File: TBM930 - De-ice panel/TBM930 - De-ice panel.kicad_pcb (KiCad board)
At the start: 2 copper layers, 190.5 x 101.6 mm, 81 parts, among them J1 SW_AIRFRAME_DE_ICE, J10 AVR-ISP-6, J2 SW_ICE_LIGHT, J3 SW_PROP_DE_ICE, J4 SW_WIND_SHIELD, J5 SW_PITOT_L_HTR, J6 SW_PITOT_R_HTR, J7 SW_INERT_SEP, J8 Barrel_Jack, J9 USB_B_Micro, SW1 SW_Push, SW2 SW_Push, U1 TLC5917IN, U2 TLC5917IN, U3 ATmega32U4-MU, Y1 16MHz

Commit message: Everything is routed!
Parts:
- removed the C1 at (214.0, 125.1)
- removed the C1 at (160.8, 130.6)
- removed C11, C14: 1uF, Capacitor_SMD:C_0603_1608Metric
- removed C12, C15: 0.1uF, Capacitor_SMD:C_0603_1608Metric
- removed C13: 10uF, Capacitor_SMD:C_0603_1608Metric
- removed D17: LED, LED_SMD:LED_1206_3216Metric_Pad1.42x1.75mm_HandSolder
- added C1: 10uF, Capacitor_SMD:C_0603_1608Metric, B.Cu at (214.0, 125.1)
- added R9: 330, Resistor_SMD:R_0603_1608Metric, B.Cu at (175.1, 131.6)
- FB1: value Ferrite_Bead -> Ferrite_Bead_Small; footprint Resistor_SMD:R_0805_2012Metric -> Capacitor_SMD:C_0805_2012Metric; moved to B.Cu
- R2, R5: footprint Resistor_SMD:R_0201_0603Metric -> Resistor_SMD:R_0603_1608Metric
- Y1: value 16MHz -> Crystal_GND24
- moved D18 95.2 mm to (182.2, 46.4)
- moved D20 95.2 mm to (87.0, 46.4)
- moved D21 95.2 mm to (182.2, 140.3)
- moved D23 95.2 mm to (87.0, 140.3)
- moved D12 63.9 mm to (160.0, 78.1)
- moved FB1 61.2 mm to (223.5, 125.3)
- moved C6 52.7 mm to (209.9, 119.8)
- moved D24 50.8 mm to (43.2, 67.9)
- moved D25 50.8 mm to (43.2, 118.7)
- moved D15 50.8 mm to (210.8, 78.1)
- moved D13 25.4 mm to (134.6, 78.1)
- moved D14 25.4 mm to (109.2, 78.1)
- moved J10 25.2 mm to (180.9, 132.0)
- moved C10 24.7 mm to (221.6, 125.3), turned to 270 degrees
- moved D2 22.2 mm to (197.9, 134.6)
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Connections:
- D16 pad 1: Net-(D16-Pad1) -> BACKLIGHT3
- FB1 pad 1: +12V_LED -> +5V
- FB1 pad 2: /+12V -> Net-(FB1-Pad2)
- J8 pad 1: /+12V -> +12V_LED
- J9 pad 1: +5V -> Net-(FB1-Pad2)
- SW2 pad 1: /~RESET -> Net-(R9-Pad1)
- U1 pad 10: Net-(U1-Pad10) -> PROP
- U1 pad 11: Net-(U1-Pad11) -> WINDSHIELD_1
- U1 pad 12: Net-(U1-Pad12) -> WINDSHIELD_2
- U1 pad 5: WINDSHIELD_2 -> Net-(U1-Pad5)
- U1 pad 6: WINDSHIELD_1 -> Net-(U1-Pad6)
- U1 pad 7: PROP -> Net-(U1-Pad7)
- U1 pad 8: AIRFRAME_2 -> AIRFRAME_1
- U1 pad 9: AIRFRAME_1 -> AIRFRAME_2
- U2 pad 10: BACKLIGHT6 -> BACKLIGHT2
- U2 pad 11: BACKLIGHT7 -> BACKLIGHT3
- U2 pad 5: BACKLIGHT1 -> BACKLIGHT5
- U2 pad 6: BACKLIGHT2 -> BACKLIGHT6
- U2 pad 7: BACKLIGHT3 -> BACKLIGHT4
- U2 pad 8: BACKLIGHT4 -> BACKLIGHT7
- U2 pad 9: BACKLIGHT5 -> BACKLIGHT1
- U3 pad 12: SW_LTS_TEST -> Net-(U3-Pad12)
- U3 pad 18: SW_PITOT_R -> /D3
- U3 pad 25: LED_CLOCK -> LED_LATCH
- U3 pad 26: LED_LATCH -> LED_CLOCK
- U3 pad 36: /A0 -> SW_LTS_TEST
- U3 pad 37: /A1 -> SW_PROP
- U3 pad 38: SW_PROP -> SW_WINDSHIELD
- U3 pad 39: SW_INERT_SEP -> SW_PITOT_L
- U3 pad 40: SW_PITOT_L -> SW_PITOT_R
- U3 pad 41: SW_WINDSHIELD -> SW_INERT_SEP
- Y1 pad 2: /XTAL2 -> GND
- Y1 pad 3: (no net) -> /XTAL2
- Y1 pad 4: (no net) -> GND
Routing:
- net +12V_LED: track 0.00 -> 545.9 mm, vias 0 -> 2
- net BACKLIGHT7: track 0.00 -> 315.9 mm, vias 0 -> 1
- net +5V: track 73.3 -> 377.1 mm, vias 6 -> 8
- net BACKLIGHT4: track 0.00 -> 174.0 mm, vias 0 -> 1
- net SW_AIRFRAME: track 0.00 -> 153.3 mm
- net AIRFRAME_1: track 0.00 -> 127.8 mm, vias 0 -> 4
- net SW_ICE_LIGHT: track 0.00 -> 127.7 mm
- net SW_LTS_TEST: track 2.97 -> 124.1 mm
- net SW_PROP: track 0.00 -> 108.3 mm
- net AIRFRAME_2: track 0.00 -> 107.7 mm, vias 0 -> 2
- net BACKLIGHT3: track 0.00 -> 105.5 mm, vias 0 -> 7
- net LED_LATCH: track 0.00 -> 99.3 mm
- net BACKLIGHT_BRIGHT: track 0.00 -> 96.6 mm, vias 0 -> 2
- net LED_CLOCK: track 0.00 -> 94.9 mm, vias 0 -> 2
- net SW_WINDSHIELD: track 0.00 -> 83.4 mm
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
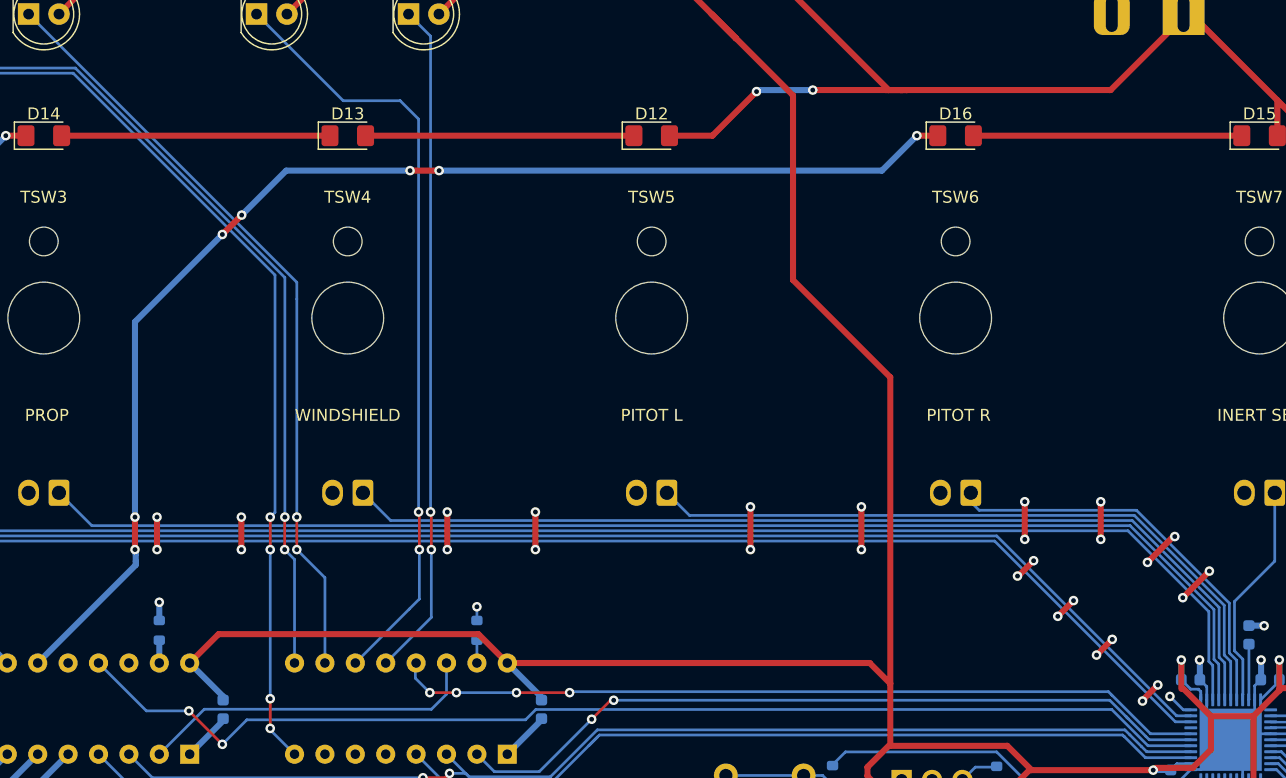
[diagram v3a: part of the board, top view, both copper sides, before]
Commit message: Schematic submitted to microtype
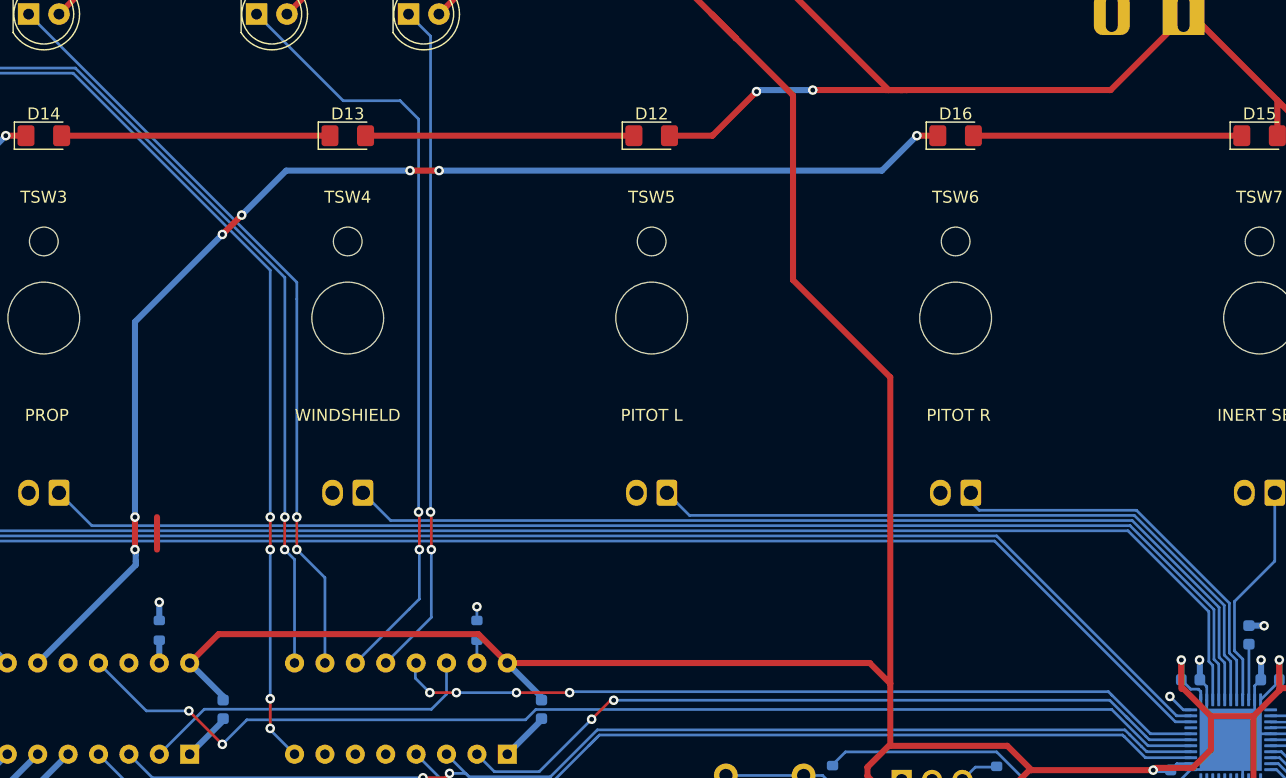
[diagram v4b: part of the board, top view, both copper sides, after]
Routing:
- net GND: track 120.0 -> 82.8 mm, vias 47 -> 19

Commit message: Schematic updates based on MT engineering discord feedback
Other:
- board text added: "JLCJLCJLCJLC"

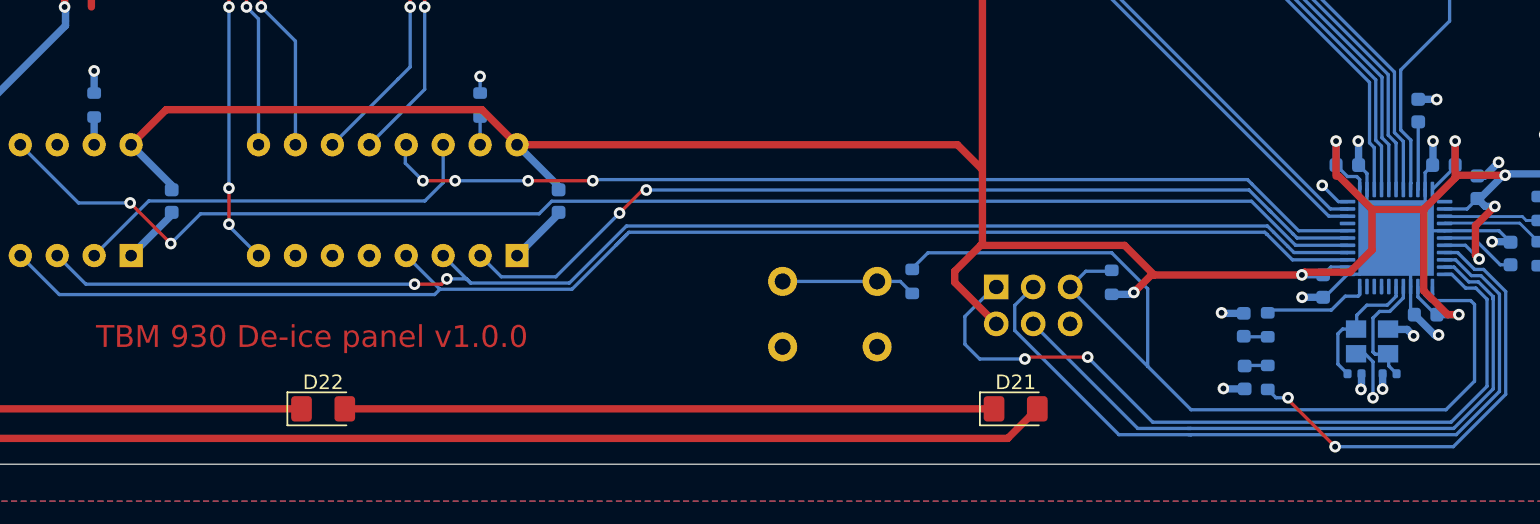
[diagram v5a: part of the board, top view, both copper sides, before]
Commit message: Additional reset components
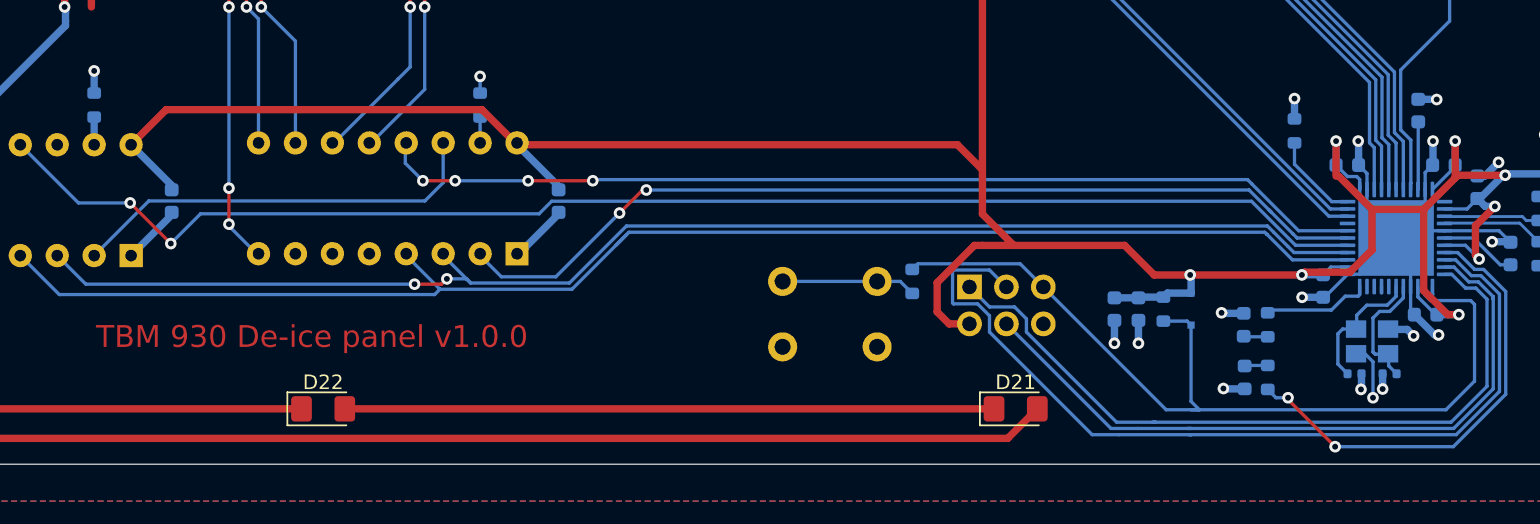
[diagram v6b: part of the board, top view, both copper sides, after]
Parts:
- removed R1: 10K, Resistor_SMD:R_0603_1608Metric
- added C11: 0.1uf, Capacitor_SMD:C_0603_1608Metric, B.Cu at (190.7, 133.5)
- added C12: 0.1uF, Capacitor_SMD:C_0603_1608Metric, B.Cu at (189.0, 133.5)
- added D17: D, Diode_SMD:D_SOD-323F, B.Cu at (194.3, 133.5)
- added R10: 10K, Resistor_SMD:R_0603_1608Metric, B.Cu at (192.4, 133.5)
- added R11: 10K, Resistor_SMD:R_0603_1608Metric, B.Cu at (201.4, 121.2)
- moved J10 1.84 mm to (179.1, 132.0)
- moved U1 0.13 mm to (148.0, 129.7)
- turned R3 to 270 degrees
- turned R4 to 270 degrees
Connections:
- net /~RESET renamed RESET
- R3 pad 1: Net-(R3-Pad1) -> GND
- R3 pad 2: GND -> Net-(R3-Pad2)
- R4 pad 1: Net-(R4-Pad1) -> GND
- R4 pad 2: GND -> Net-(R4-Pad2)
- U1 pad 15: Net-(R3-Pad1) -> Net-(R3-Pad2)
- U2 pad 15: Net-(R4-Pad1) -> Net-(R4-Pad2)
- U3 pad 33: GND -> Net-(R11-Pad1)
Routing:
- net /SCK: track 52.7 -> 61.3 mm
- net Net-(R11-Pad1): track 0.00 -> 6.18 mm
- net RESET: track 68.1 -> 62.0 mm
- net +5V: track 377.1 -> 382.5 mm
- net /MISO: track 53.8 -> 50.8 mm, vias 2 -> 0
- net GND: track 82.8 -> 85.1 mm, vias 19 -> 21
- net Net-(R4-Pad2): track 0.00 -> 1.91 mm
- net Net-(R4-Pad1): track 1.91 -> 0.00 mm
- net Net-(R3-Pad1): track 1.91 -> 0.00 mm
- net /MOSI: track 46.7 -> 48.5 mm
- net Net-(R3-Pad2): track 0.00 -> 1.78 mm

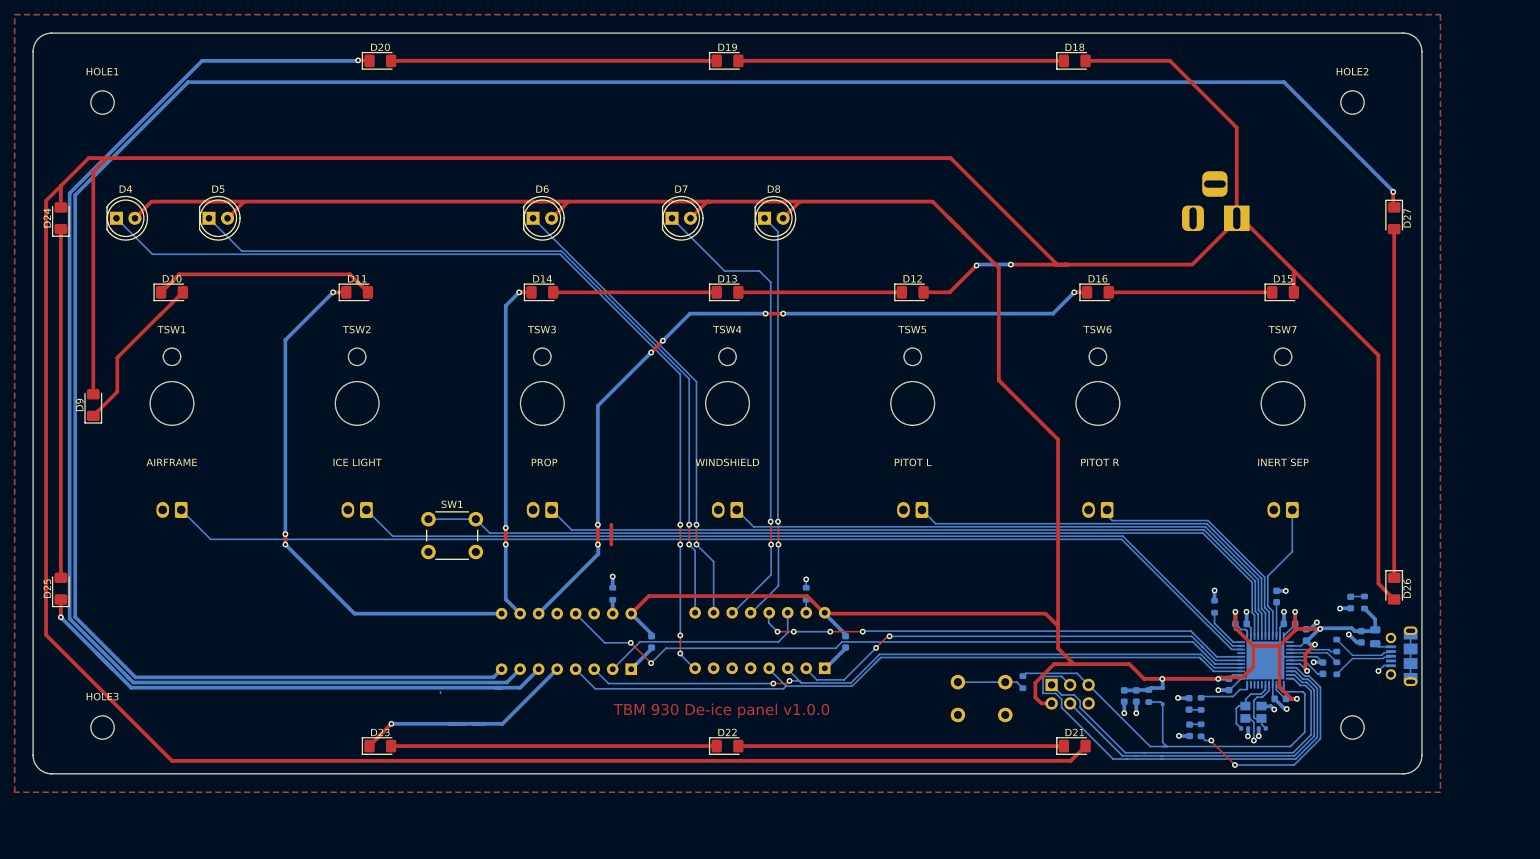
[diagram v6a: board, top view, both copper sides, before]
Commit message: Fix 12V routing
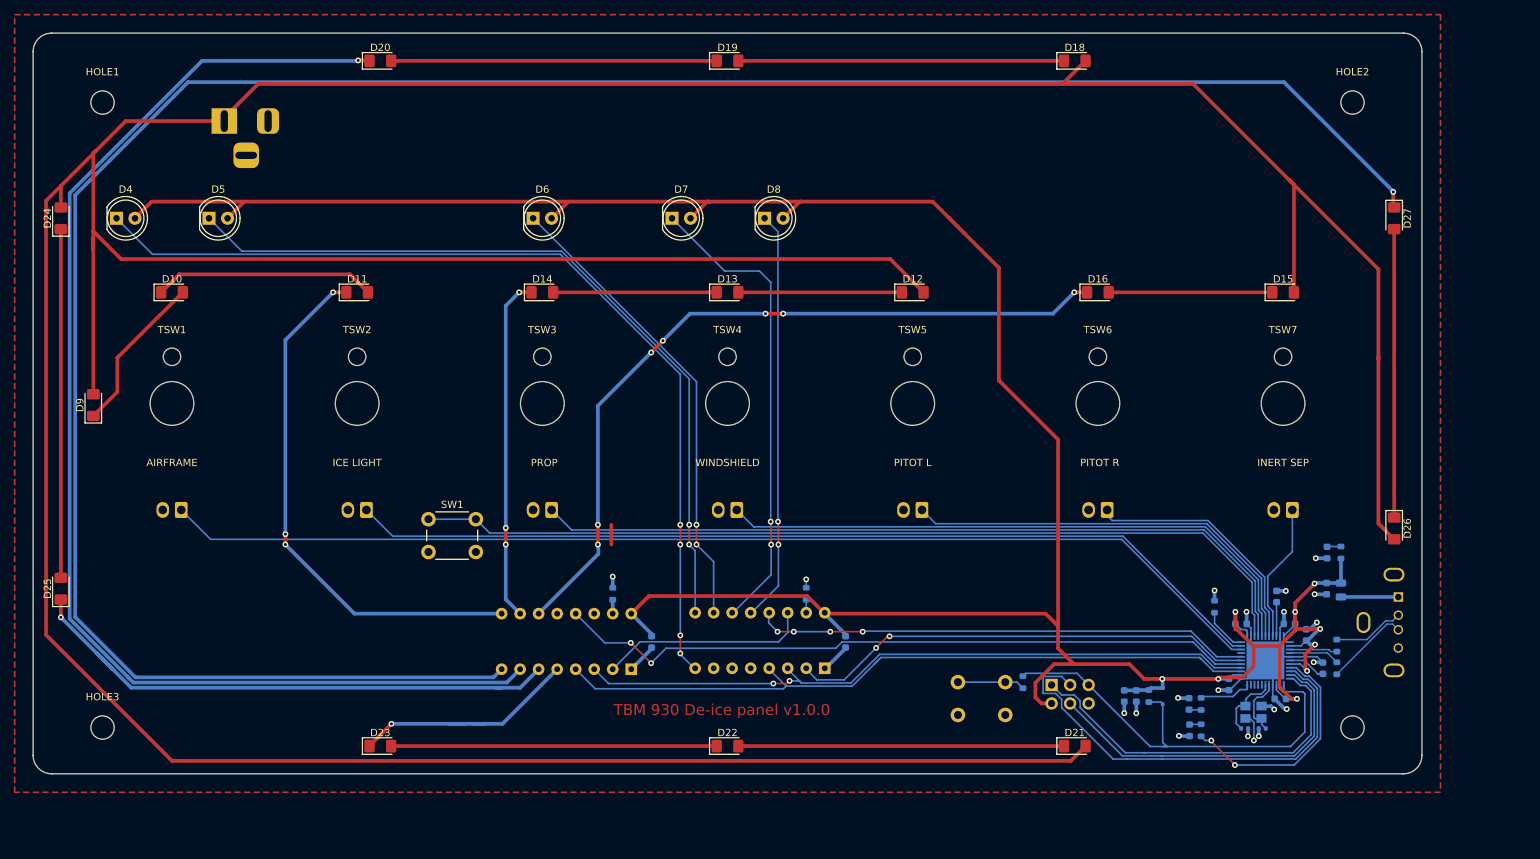
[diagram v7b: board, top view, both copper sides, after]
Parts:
- J9: footprint Connector_USB:USB_Micro-B_Molex-105017-0001 -> Global MobiFlight panel parts:USB_A_Molex_105057_Vertical
- moved J8 139.5 mm to (65.6, 54.6), turned to 180 degrees
- moved D26 8.26 mm to (226.1, 110.5)
- moved C10 8.14 mm to (216.8, 118.7)
- moved J9 8.14 mm to (226.6, 119.9)
- moved FB1 7.95 mm to (218.8, 118.9)
- moved D3 7.58 mm to (216.9, 113.8)
- moved R6 7.58 mm to (218.8, 113.8)
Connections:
- net Net-(FB1-Pad2) renamed /VBUS
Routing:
- net +12V_LED: track 545.9 -> 624.6 mm, vias 2 -> 0
- net GND: track 85.1 -> 76.8 mm, vias 21 -> 20
- net Net-(D26-Pad1): track 47.8 -> 39.6 mm
- net /VBUS: track 2.33 -> 7.88 mm
- net /DR+: track 8.45 -> 11.6 mm
- net /DR-: track 8.54 -> 9.83 mm
- net +5V: track 382.5 -> 383.2 mm, vias 8 -> 9
